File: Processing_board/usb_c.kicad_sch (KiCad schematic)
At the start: 12 parts, among them J2 USB_C_Receptacle_USB2.0_16P, U5 MCP2210x-SO, Y1 HC49US-FF3F18 12MHz

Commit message: the 2nd (hopefully final) version of circuit diagram
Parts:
- removed C5: 1 uF, symbol Device:C_Small
- added R1: 10k, symbol Device:R
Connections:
- net *CS: now also R1.2
- net GND: now also C4.1; no longer C4.2
- net VBUS: no longer R5.1, U5.1 (VDD)
- net 3.3V: now reaches U5.17 (VUSB)
- net 3.3V: now also C4.2, R5.1, U5.1 (VDD), R1.1; no longer C4.1
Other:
- note added: "Pull-up"
- note removed: "Note : I chose 1 uF RANDOMLY for C5 because datasheet says "the total effective capacitance appearing across VBUS and ground must be no more than 10 µF""
- moved on the sheet: C4

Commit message: added reset button
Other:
- company: (none) -> N-Pulse
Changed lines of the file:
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@@
 	(generator_version "9.0")
 	(paper "A4")
+	(title_block
+		(company "N-Pulse")
+	)
 	(text "Note : R5 can be from 1 to 10k to use the Power-On-Reset\ncircuitry of the chip. I chose 5.1k because we already have\nothers\n"
 		(exclude_from_sim no)

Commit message: addressed all reviews except the LDO 5V
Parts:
- removed R1: 10k, symbol Device:R
- removed R5: 5.1k, symbol Device:R
- removed R6: 116 Ohm, symbol Device:R
- removed U5: MCP2210x-SO, Package_SO:SOIC-20W_7.5x12.8mm_P1.27mm, symbol Interface_USB:MCP2210x-SO
- added C2: 220nF, symbol Device:C_Small
- added D5: IN_S42BT LED, symbol Device:LED
- added IC3: MCP2200-I_SO, SOIC127P1030X265-20N, symbol MCP2200-I_SO:MCP2200-I_SO
- added Q1, Q2: NMOS, symbol Simulation_SPICE:NMOS
- added R1, R10, R11: 10k, symbol Device:R_Small
- added R5: 100R, symbol Device:R_Small
- C4: value 220nF -> 470nF
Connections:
- net 3.3V: now also C2.1, IC3.1 (VDD), IC3.17 (VUSB), R1.1, R10.1, R5.2
- net GND: now also C2.2, IC3.20 (VSS), Q1.3 (S), Q2.3 (S), R11.2; no longer D3.1 (K)
- net VBUS: now also Q1.2 (G), R11.1
- net at C6.2, Y1.1: now also IC3.3 (OSC2)
- net at C7.2, Y1.2: now also IC3.2 (OSC1)
- net at D3.2 (A): now also D5.2 (A), R5.1
- net at J2.A7 (D-), J2.B7 (D-): now also IC3.18 (D-)
- net at J2.A6 (D+), J2.B6 (D+): now also IC3.19 (D+)
- new net: IC3.4 (~{RST}), Q2.1 (D), R10.2
- new net: D3.1 (K), IC3.5 (GP7/TXLED)
- new net: D5.1 (K), IC3.6 (GP6/RXLED)
- new net: Q1.1 (D), Q2.2 (G), R1.2
- new net RX: IC3.12 (RX)
- new net TX: IC3.10 (TX)
- no-connect marks 0 -> 10
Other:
- note added: "CTS and RTS not useful Other GPIO pins not useful"
- note added: "Cl = 2*(18-4) = 28 pF"
- note added: "GP6/7 are active low, so we need this config so that LED shines when RX/TX is active"
- note added: "Have to decide which transistor to use. Any NMOS should work normally"
- note added: "LED has 2.1-2.4V voltage drop Vf and can handle 25mA max with 100Ohm, should have ~10mA"
- note added: "Pull-down and pull-up resistor values have been chosen (pretty arbitrarily) at 10k"
- note added: "SBU pins are for USB "alternate mode" since we don't use it, we leave them floating"
- note added: "Since UART can not receive & transmit at the same time, sharing R isn't a problem ?"
- note removed: "Chip select"
- note removed: "Note : R5 can be from 1 to 10k to use the Power-On-Reset circuitry of the chip. I chose 5.1k because we already have others"
- note removed: "Pull-up"
- note removed: "This LED indicate SPI transfer (on = idle, off=transfer) if GP3 is software-activated as SPI traffic pin"
- moved on the sheet: C4, C6, C7, D3, J2, R3, R4, Y1

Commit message: 3 RF antennas
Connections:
- net 3.3V renamed +3.3V
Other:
- note added: "LED has 2.1-2.4V voltage drop Vf and can handle 25mA max with 100R, should have ~10mA"
- note removed: "LED has 2.1-2.4V voltage drop Vf and can handle 25mA max with 100Ohm, should have ~10mA"
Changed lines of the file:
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@@
 		)
 	)
-	(text "LED has 2.1-2.4V voltage drop Vf\nand can handle 25mA max\nwith 100Ohm, should have ~10mA"
+	(text "LED has 2.1-2.4V voltage drop Vf\nand can handle 25mA max\nwith 100R, should have ~10mA"
 		(exclude_from_sim no)
 		(at 206.248 117.348 0)
@@
 			(width 0)
 			(type default)
-		)
-	)
-	(global_label "3.3V"
-		(shape input)
-		(at 171.45 48.26 90)
-		(fields_autoplaced yes)
-		(effects
-			(font
-				(size 1.27 1.27)
-			)
-			(justify left)
-		)
-		(property "Intersheetrefs" "${INTERSHEET_REFS}"
-			(at 171.45 41.1624 90)
-			(effects
-				(font
-					(size 1.27 1.27)
-				)
-				(justify left)
-				(hide yes)
-			)
-		)
-	)
-	(global_label "3.3V"
-		(shape input)
-		(at 222.25 101.6 0)
-		(fields_autoplaced yes)
-		(effects
-			(font
-				(size 1.27 1.27)
-			)
-			(justify left)
-		)
-		(property "Intersheetrefs" "${INTERSHEET_REFS}"
-			(at 229.3476 101.6 0)
-			(effects
-				(font
-					(size 1.27 1.27)
-				)
-				(justify left)
-				(hide yes)
-			)
 		)
 	)
@@
 	)
 	(symbol
+		(lib_id "power:+3.3V")
+		(at 171.45 48.26 0)
+		(unit 1)
+		(exclude_from_sim no)
+		(in_bom yes)
+		(on_board yes)
+		(dnp no)
+		(fields_autoplaced yes)
+		(property "Reference" "#PWR051"
+			(at 171.45 52.07 0)
+			(effects
+				(font
+					(size 1.27 1.27)
+				)
+				(hide yes)
+			)
+		)
+		(property "Value" "+3.3V"
+			(at 171.45 43.18 0)
+			(effects
+				(font
+					(size 1.27 1.27)
+				)
+			)
+		)
+		(property "Footprint" ""
+			(at 171.45 48.26 0)
+			(effects
+				(font
+					(size 1.27 1.27)
+				)
+				(hide yes)
+			)
+		)
+		(property "Datasheet" ""
+			(at 171.45 48.26 0)
+			(effects
+				(font
+					(size 1.27 1.27)
+				)
+				(hide yes)
+			)
+		)
+		(property "Description" "Power symbol creates a global label with name \"+3.3V\""
+			(at 171.45 48.26 0)
+			(effects
+				(font
+					(size 1.27 1.27)
+				)
+				(hide yes)
+			)
+		)
+		(pin "1"
+		)
+		(instances
+			(project "Processing_board"
+				(path "/b48cfd4a-6c36-4270-b2b4-45cb26e35477/db67a34e-d5f8-42fb-9749-5806aa4cd127"
+					(reference "#PWR051")
+					(unit 1)
+				)
+			)
+		)
+	)
+	(symbol
 		(lib_id "Device:Crystal")
 		(at 147.32 92.71 90)
@@
 					(unit 1)
 				)
+			)
+		)
+	)
+	(symbol
+		(lib_id "power:+3.3V")
+		(at 222.25 101.6 0)
+		(unit 1)
+		(exclude_from_sim no)
+		(in_bom yes)
+		(on_board yes)
+		(dnp no)
+		(fields_autoplaced yes)
+		(property "Reference" "#PWR052"
+			(at 222.25 105.41 0)
+			(effects
+				(font
+					(size 1.27 1.27)
+				)
+				(hide yes)
+			)
+		)
+		(property "Value" "+3.3V"
+			(at 222.25 96.52 0)
+			(effects
+				(font
+					(size 1.27 1.27)
+				)
+			)
+		)
+		(property "Footprint" ""
+			(at 222.25 101.6 0)
+			(effects
+				(font
+					(size 1.27 1.27)
+				)
+				(hide yes)
+			)
+		)
+		(property "Datasheet" ""
+			(at 222.25 101.6 0)
+			(effects
+				(font
+					(size 1.27 1.27)
+				)
+				(hide yes)
+			)
+		)
+		(property "Description" "Power symbol creates a global label with name \"+3.3V\""
+			(at 222.25 101.6 0)
+			(effects
+				(font
+					(size 1.27 1.27)
+				)
+				(hide yes)
+			)
+		)
+		(pin "1"
+		)
+		(instances
+			(project "Processing_board"
+				(path "/b48cfd4a-6c36-4270-b2b4-45cb26e35477/db67a34e-d5f8-42fb-9749-5806aa4cd127"
+					(reference "#PWR052")
+					(unit 1)
+				)

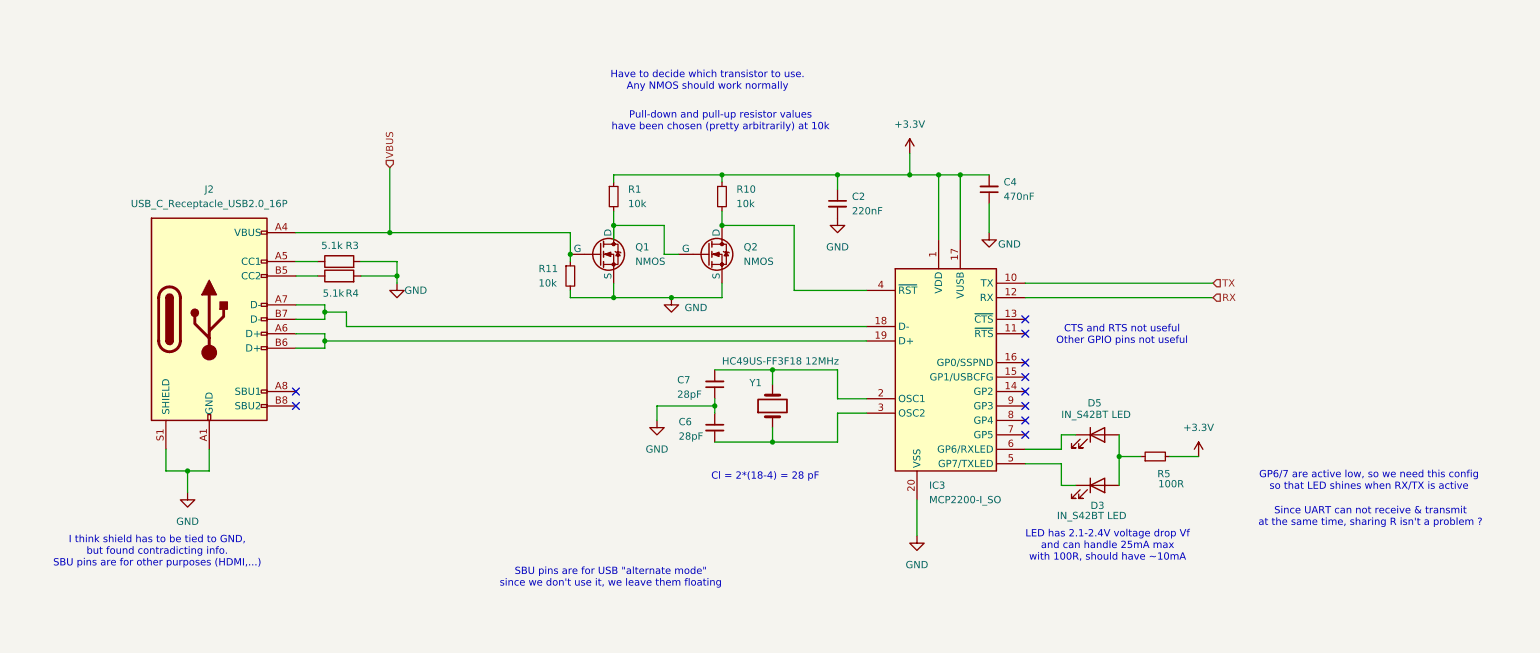
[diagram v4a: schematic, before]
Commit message: added all footprints, ready (?) to design PCB
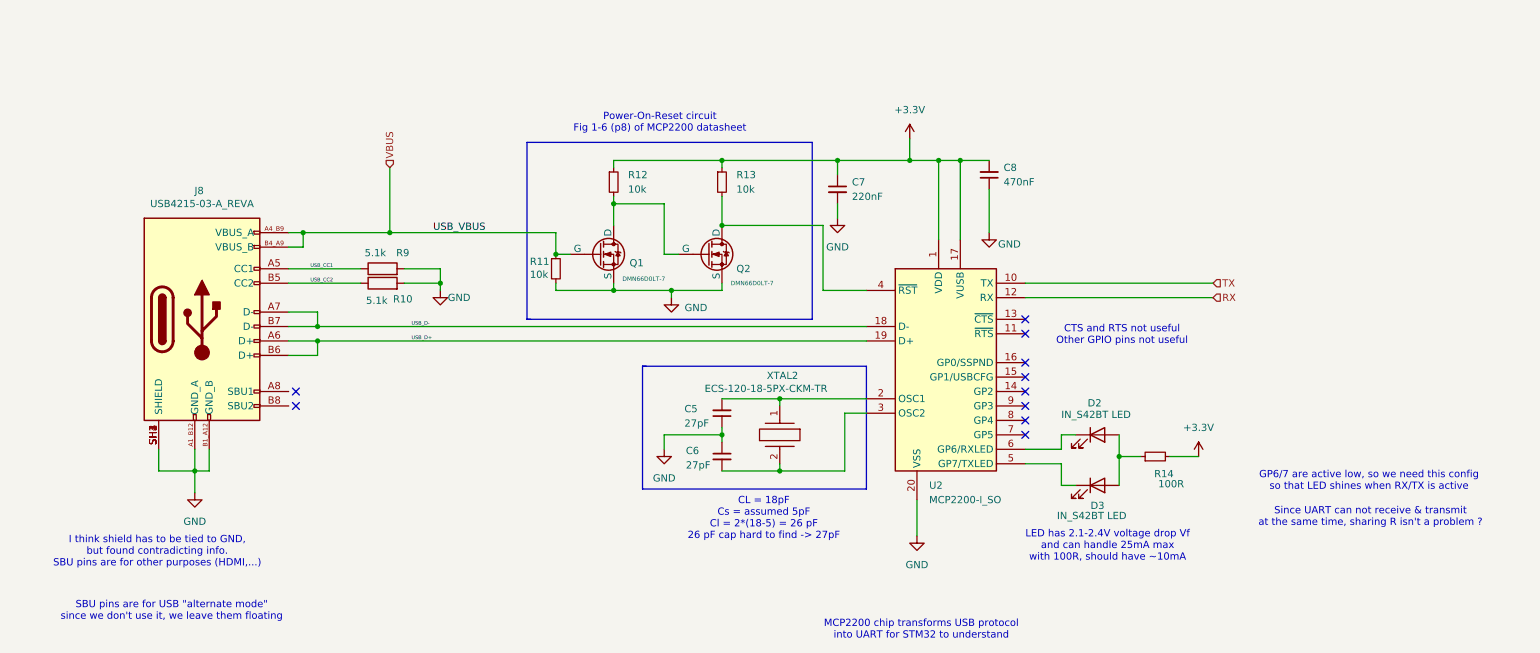
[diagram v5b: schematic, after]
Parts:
- removed J2: USB_C_Receptacle_USB2.0_16P, symbol Connector:USB_C_Receptacle_USB2.0_16P
- removed Y1: HC49US-FF3F18 12MHz, symbol Device:Crystal
- added J8: USB4215-03-A_REVA, USB4215_03_A:GCT_USB4215-03-A_REVA, symbol USB4215-03-A_REVA:USB4215-03-A_REVA
- added XTAL2: ECS-120-18-5PX-CKM-TR, ECS-120-18-5PX-CKM-TR:ECS120185PXCKMTR, symbol ECS-120-18-5PX-CKM-TR:ECS-120-18-5PX-CKM-TR
- C5: renamed from C7; value 28pF -> 27pF; footprint (none) -> Capacitor_SMD:C_0805_2012Metric
- C6: value 28pF -> 27pF; footprint (none) -> Capacitor_SMD:C_0805_2012Metric
- C7: renamed from C2; footprint (none) -> Capacitor_SMD:C_0402_1005Metric
- C8: renamed from C4; footprint (none) -> Capacitor_SMD:C_0402_1005Metric
- D2: renamed from D5; footprint (none) -> LED_SMD:LED_0402_1005Metric
- D3: footprint (none) -> LED_SMD:LED_0402_1005Metric
- Q1, Q2: value NMOS -> DMN66D0LT-7; footprint (none) -> DMN66D0LT-7:SOT50P160X90-3N; Description_1 (none) -> Trans MOSFET N-CH 60V 0.115A 3-Pin SOT-523 T/R; Height (none) -> 0.9; Manufacturer_Name (none) -> Diodes Incorporated; Manufacturer_Part_Number (none) -> DMN66D0LT-7; Mouser Part Number (none) -> 621-DMN66D0LT-7; Mouser Price/Stock (none) -> https://www.mouser.co.uk/ProductDetail/Diodes-Incorporated/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
- R10: renamed from R4; footprint (none) -> Resistor_SMD:R_0402_1005Metric
- R11: footprint (none) -> Resistor_SMD:R_0402_1005Metric
- R12: renamed from R1; footprint (none) -> Resistor_SMD:R_0402_1005Metric
- R13: renamed from R10; footprint (none) -> Resistor_SMD:R_0402_1005Metric
- R14: renamed from R5; footprint (none) -> Resistor_SMD:R_0402_1005Metric
- R9: renamed from R3; footprint (none) -> Resistor_SMD:R_0402_1005Metric
- U2: renamed from IC3; footprint SOIC127P1030X265-20N -> MCP2200-I_SO:SOIC127P1030X265-20N
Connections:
- net GND: now also J8.A1_B12 (GND_A), J8.B1_A12 (GND_B), J8.SH1 (SHIELD), J8.SH2 (SHIELD), J8.SH3 (SHIELD), J8.SH4 (SHIELD)
- net VBUS: now also J8.A4_B9 (VBUS_A), J8.B4_A9 (VBUS_B)
- net at C6.2, U2.3 (OSC2): now also XTAL2.2
- net at C5.2, U2.2 (OSC1): now also XTAL2.1
- net USB_D-: now reaches U2.18 (D-)
- net USB_D-: now also J8.A7 (D-), J8.B7 (D-)
- net USB_D+: now reaches U2.19 (D+)
- net USB_D+: now also J8.A6 (D+), J8.B6 (D+)
- net USB_CC2: now reaches R10.1
- net USB_CC2: now also J8.B5 (CC2)
- net USB_CC1: now reaches R9.1
- net USB_CC1: now also J8.A5 (CC1)
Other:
- note added: "CL = 18pF Cs = assumed 5pF Cl = 2*(18-5) = 26 pF 26 pF cap hard to find -> 27pF"
- note added: "MCP2200 chip transforms USB protocol into UART for STM32 to understand"
- note added: "Power-On-Reset circuit Fig 1-6 (p8) of MCP2200 datasheet"
- note removed: "Cl = 2*(18-4) = 28 pF"
- note removed: "Have to decide which transistor to use. Any NMOS should work normally"
- note removed: "Pull-down and pull-up resistor values have been chosen (pretty arbitrarily) at 10k"
- moved on the sheet: C5, C6, C7, C8, R10, R11, R12, R13, R9

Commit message: first draft of PCB almost done
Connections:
- net MCP_NRST: now reaches Q2.1 (D), R13.2, U2.4 (~{RST})
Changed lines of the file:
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@@
 	)
 	(no_connect
-		(at 63.5 92.71)
+		(at 62.23 90.17)
+	)
+	(no_connect
+		(at 62.23 92.71)
 	)
 	(no_connect
@@
 	(no_connect
 		(at 191.77 92.71)
-	)
-	(no_connect
-		(at 63.5 90.17)
 	)
 	(no_connect
@@
 		(effects
 			(font
+				(size 0.635 0.635)
+			)
+			(justify left bottom)
+		)
+	)
+	(label "MCP_NRST"
+		(at 143.51 60.96 0)
+		(effects
+			(font

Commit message: more minor cleanup
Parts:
- added TP2: TestPoint, TestPoint:TestPoint_Pad_D1.0mm, symbol Connector:TestPoint
- added TP3, TP4: PN5260, PN5260:PN5260, symbol PN5260:5260
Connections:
- net RX: now also TP4.1
- net TX: now also TP3.1
- net at C6.2, U2.3 (OSC2), XTAL2.2: now also TP2.1
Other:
- note added: "12 MHz Oscillator"

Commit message: more cleanup
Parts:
- renumbered C5 to C85, C6 to C87, C7 to C90, C8 to C92, D2 to D10, D3 to D11, J8 to J14, Q1 to Q4, Q2 to Q6, R9 to R23, R10 to R24, R11 to R28, R12 to R29, R13 to R30, R14 to R34, TP2 to TP18, TP3 to TP20, TP4 to TP21, U2 to U16, XTAL2 to XTAL3
